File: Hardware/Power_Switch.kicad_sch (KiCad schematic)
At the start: 3 parts, among them J1 THROTTLE

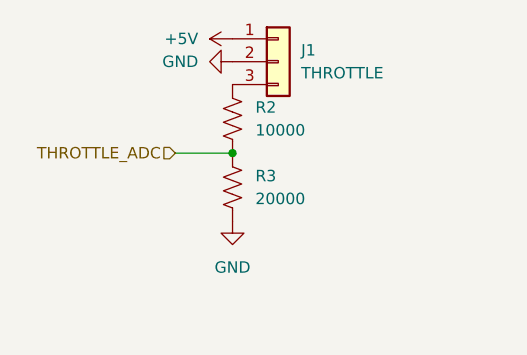
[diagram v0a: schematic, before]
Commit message: Restructure VCU schema
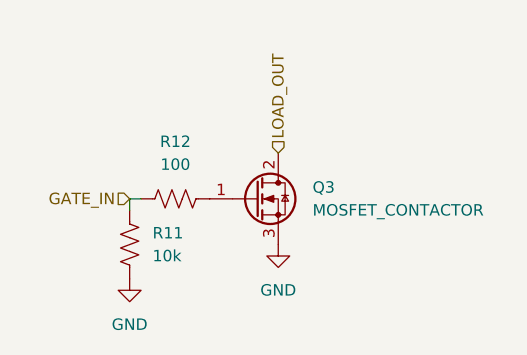
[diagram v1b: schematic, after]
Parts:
- removed J1: THROTTLE, symbol Connector_Generic:Conn_01x03
- removed R2: 10000, Package_DFN_QFN:WDFN-10-1EP_3x3mm_P0.5mm_EP1.8x2.5mm, symbol Device:R_US
- removed R3: 20000, symbol Device:R_US
- added Q3: MOSFET_CONTACTOR, Package_QFP:TQFP-44_10x10mm_P0.8mm, symbol Transistor_FET:Q_NMOS_GDS
- added R11: 10k, Package_DFN_QFN:WDFN-10-1EP_3x3mm_P0.5mm_EP1.8x2.5mm, symbol Device:R_US
- added R12: 100, Package_DFN_QFN:WDFN-10-1EP_3x3mm_P0.5mm_EP1.8x2.5mm, symbol Device:R_US
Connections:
- net GND: now also Q3.3 (S), R11.1
- new net: Q3.1 (G), R12.2
- new net GATE_IN: R11.2, R12.1
- new net LOAD_OUT: Q3.2 (D)

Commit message: Set footprint + excludes
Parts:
- Q3: footprint Package_QFP:TQFP-44_10x10mm_P0.8mm -> Package_TO_SOT_THT:TO-220-3_Vertical
- R11, R12: footprint Package_DFN_QFN:WDFN-10-1EP_3x3mm_P0.5mm_EP1.8x2.5mm -> Resistor_THT:R_Axial_DIN0207_L6.3mm_D2.5mm_P7.62mm_Horizontal
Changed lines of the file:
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@@
 			)
 		)
-		(property "Footprint" "Package_QFP:TQFP-44_10x10mm_P0.8mm"
+		(property "Footprint" "Package_TO_SOT_THT:TO-220-3_Vertical"
 			(at 129.54 96.52 0)
 			(hide yes)
@@
 			)
 		)
-		(property "Footprint" "Package_DFN_QFN:WDFN-10-1EP_3x3mm_P0.5mm_EP1.8x2.5mm"
+		(property "Footprint" "Resistor_THT:R_Axial_DIN0207_L6.3mm_D2.5mm_P7.62mm_Horizontal"
 			(at 115.824 98.044 90)
 			(hide yes)
@@
 			)
 		)
-		(property "Footprint" "Package_DFN_QFN:WDFN-10-1EP_3x3mm_P0.5mm_EP1.8x2.5mm"
+		(property "Footprint" "Resistor_THT:R_Axial_DIN0207_L6.3mm_D2.5mm_P7.62mm_Horizontal"
 			(at 109.474 103.886 90)
 			(hide yes)
